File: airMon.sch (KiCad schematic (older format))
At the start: 0 parts

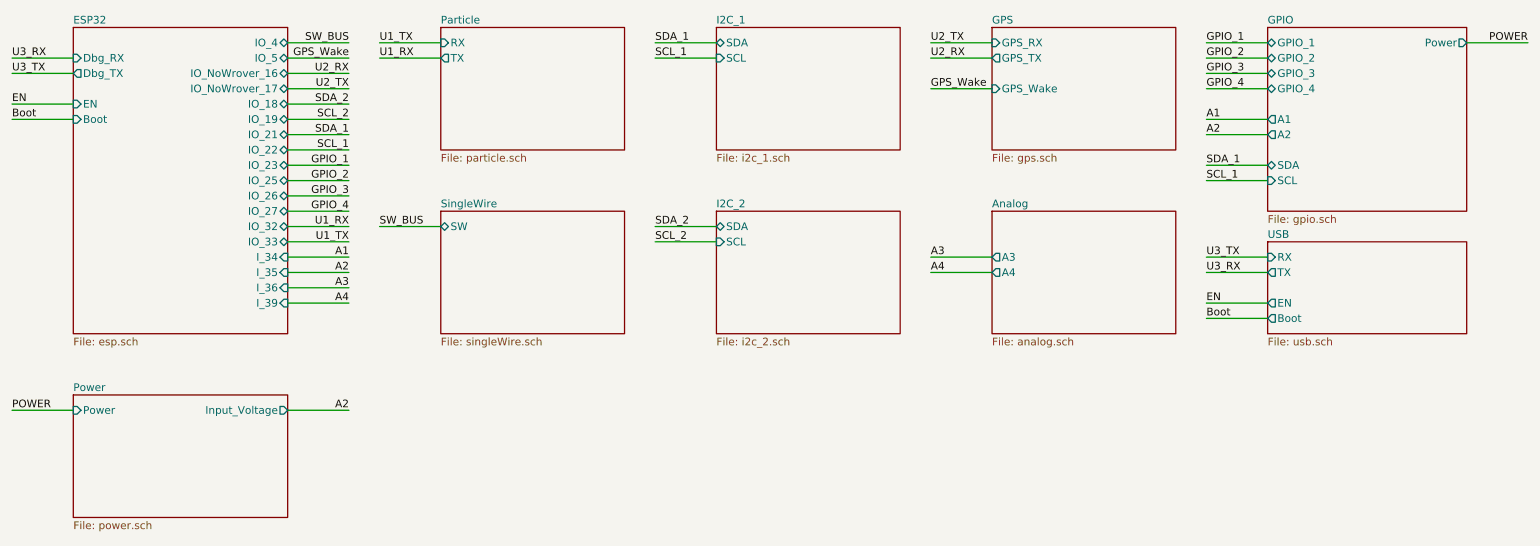
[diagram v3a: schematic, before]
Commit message: Added RFM95 Module for Lora Added Changelog Changed input voltage monitoring from A2(IO35) to A3(IO36) Removed A3 12V compatibility Rearranged IOs to fit new components
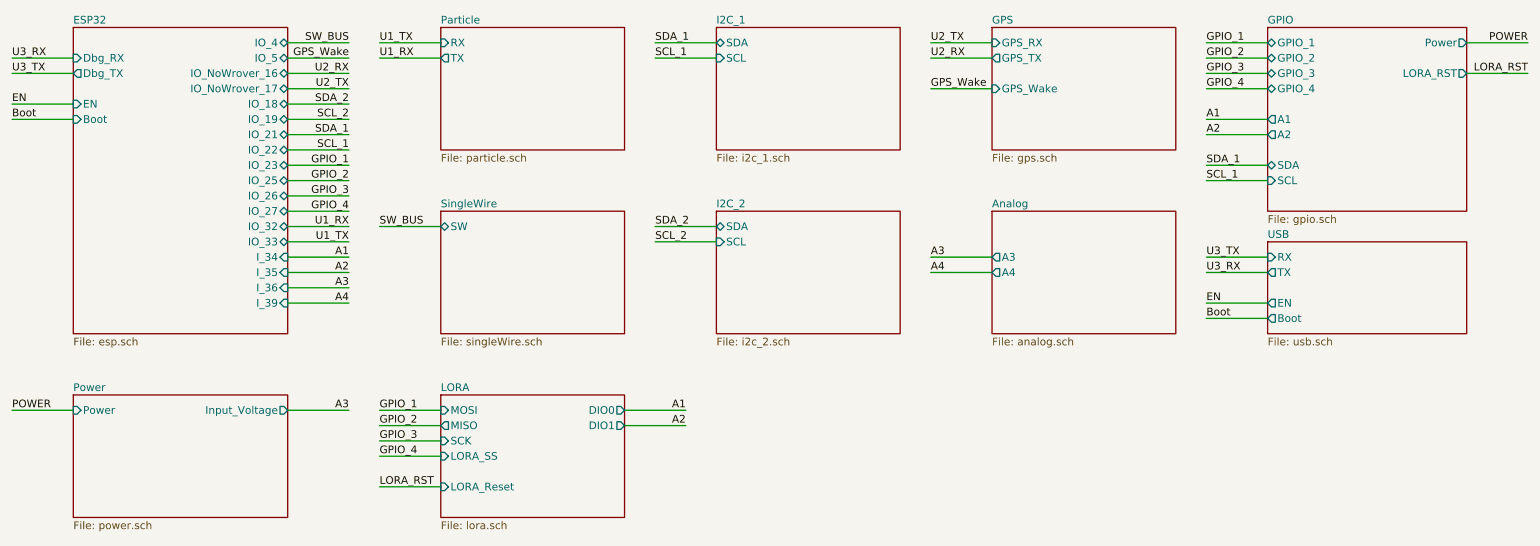
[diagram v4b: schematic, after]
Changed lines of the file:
@@
 $Descr A4 11693 8268
 encoding utf-8
-Sheet 1 11
+Sheet 1 12
 Title "AirMon"
 Date "2020-01-17"
@@
 F9 "SCL" I L 9000 3000 50
 F10 "Power" O R 10300 2100 50
+F11 "LORA_RST" O R 10300 2300 50
 $EndSheet
 Wire Wire Line
@@
 Text Label 800  2200 0    50   ~ 0
 U3_RX
+$Sheet
+S 3600 4400 1200 800
+U 5E22FCEF
+F0 "LORA" 50
+F1 "lora.sch" 50
+F2 "SCK" I L 3600 4700 50
+F3 "MOSI" I L 3600 4500 50
+F4 "MISO" O L 3600 4600 50
+F5 "LORA_SS" I L 3600 4800 50
+F6 "LORA_Reset" I L 3600 5000 50
+F7 "DIO0" O R 4800 4500 50
+F8 "DIO1" O R 4800 4600 50
+$EndSheet
+Wire Wire Line
+	3600 4500 3200 4500
+Text Label 3200 4500 0    50   ~ 0
+GPIO_1
+Wire Wire Line
+	3600 4600 3200 4600
+Text Label 3200 4600 0    50   ~ 0
+GPIO_2
+Wire Wire Line
+	3600 4700 3200 4700
+Text Label 3200 4700 0    50   ~ 0
+GPIO_3
+Wire Wire Line
+	3600 4800 3200 4800
+Text Label 3200 4800 0    50   ~ 0
+GPIO_4
+Wire Wire Line
+	3600 5000 3200 5000
+Text Label 3200 5000 0    50   ~ 0
+LORA_RST
+Wire Wire Line
+	10300 2300 10700 2300
+Text Label 10700 2300 2    50   ~ 0
+LORA_RST
+Wire Wire Line
+	4800 4500 5200 4500
+Text Label 5200 4500 2    50   ~ 0
+A1
+Wire Wire Line
+	4800 4600 5200 4600
+Text Label 5200 4600 2    50   ~ 0
+A2
 Wire Wire Line
 	2600 4500 3000 4500
 Text Label 3000 4500 2    50   ~ 0
-A2
+A3
 $EndSCHEMATC
